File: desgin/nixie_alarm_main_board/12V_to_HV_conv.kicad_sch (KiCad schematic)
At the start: 19 parts, among them IC1 LM3488MM, IC5 TPH5200FNH, IC8 MCP4018T-502E_LT

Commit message: filter caps
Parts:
- added R42, R43: 5.1kΩ, RESC2012X60N, symbol SamacSys_Parts:ERJ-UP6D5101V
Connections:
- net +12V: now also L2.1
- net +3.3V: now also R42.2, R43.2
- net DPOT_SCL: now also R42.1
- net DPOT_SDA: now also R43.1
- net at IC1.1 (ISEN), R13.1: no longer L2.1
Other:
- moved on the sheet: C10, D1, L2

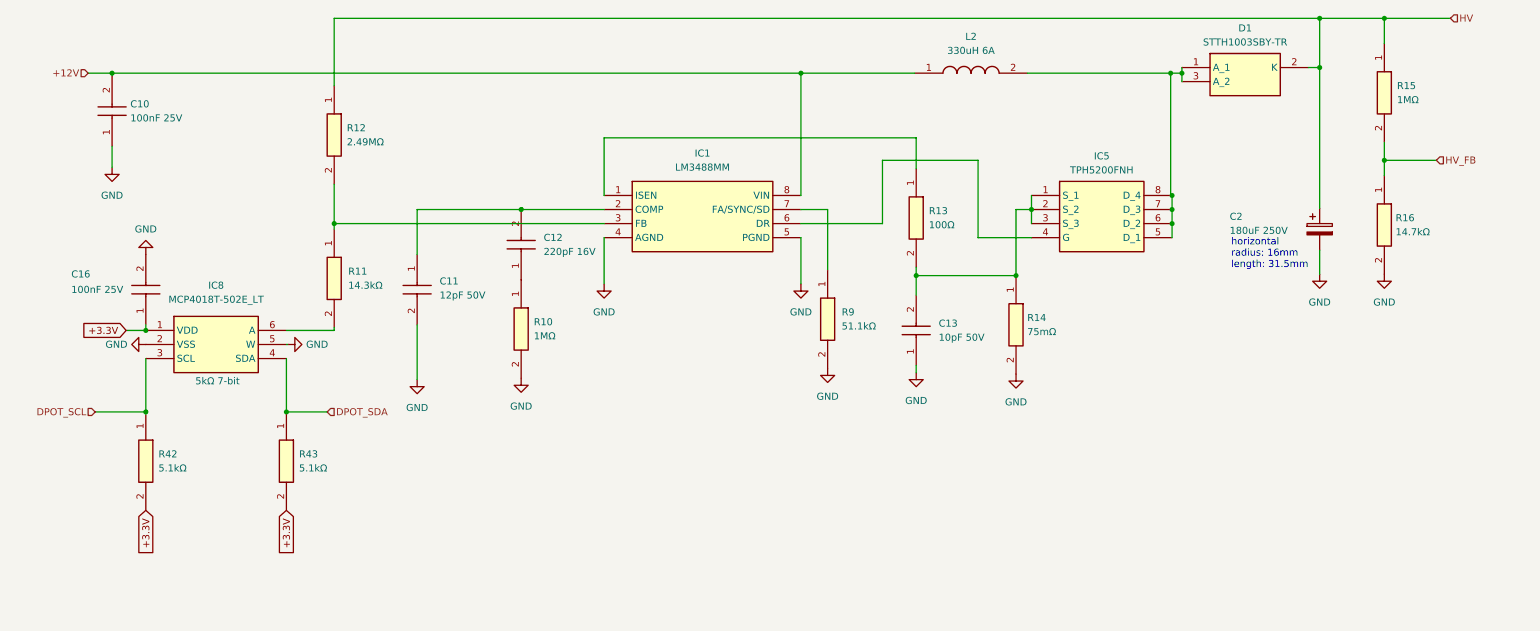
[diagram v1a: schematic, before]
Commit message: new rezistors
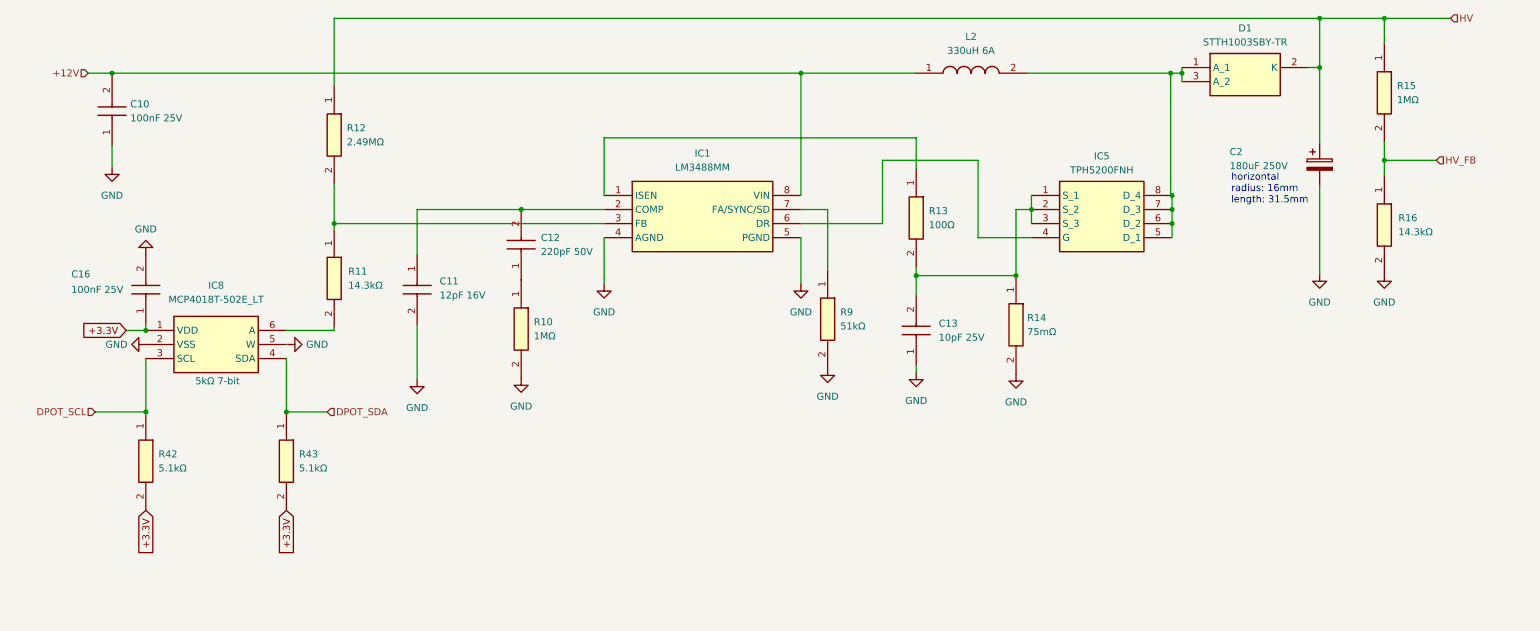
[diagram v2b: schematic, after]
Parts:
- C10, C16: footprint GRM033D70J224ME01D -> Capacitor_SMD:C_0805_2012Metric_Pad1.18x1.45mm_HandSolder
- C11: value 12pF 50V -> 12pF 16V
- C12: value 220pF 16V -> 220pF 50V; footprint GRM033D70J224ME01D -> Capacitor_SMD:C_0805_2012Metric_Pad1.18x1.45mm_HandSolder
- C13: value 10pF 50V -> 10pF 25V; footprint GRM033D70J224ME01D -> Capacitor_SMD:C_0805_2012Metric_Pad1.18x1.45mm_HandSolder
- R10, R12, R15: footprint RESC1005X40N -> Resistor_SMD:R_1206_3216Metric_Pad1.30x1.75mm_HandSolder
- R11: footprint RESC1005X40N -> Resistor_SMD:R_0805_2012Metric_Pad1.20x1.40mm_HandSolder
- R14: footprint ERJUP6 -> Resistor_SMD:R_0805_2012Metric_Pad1.20x1.40mm_HandSolder
- R16: value 14.7kΩ -> 14.3kΩ; footprint RESC1005X40N -> Resistor_SMD:R_0805_2012Metric_Pad1.20x1.40mm_HandSolder
- R42, R43: footprint RESC2012X60N -> Resistor_SMD:R_0805_2012Metric_Pad1.20x1.40mm_HandSolder
- R9: value 51.1kΩ -> 51kΩ; footprint RESC1005X40N -> Resistor_SMD:R_0805_2012Metric_Pad1.20x1.40mm_HandSolder
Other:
- moved on the sheet: C2
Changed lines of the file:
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@@
 	)
 	(junction
-		(at 247.904 52.324)
-		(diameter 0)
-		(color 0 0 0 0)
-	)
-	(junction
 		(at 29.718 53.34)
 		(diameter 0)
@@
 	)
 	(junction
+		(at 247.904 52.324)
+		(diameter 0)
+		(color 0 0 0 0)
+	)
+	(junction
 		(at 259.588 69.088)
 		(diameter 0)
@@
 	(wire
 		(pts
-			(xy 247.904 85.344) (xy 247.904 89.662)
+			(xy 247.904 73.66) (xy 247.904 89.662)
 		)
 		(stroke
@@
 	(wire
 		(pts
-			(xy 247.904 52.324) (xy 247.904 77.724)
+			(xy 247.904 52.324) (xy 247.904 66.04)
 		)
 		(stroke
@@
 	(text "horizontal\nradius: 16mm\nlength: 31.5mm\n"
 		(exclude_from_sim no)
-		(at 231.902 85.9791 0)
+		(at 231.902 74.2951 0)
 		(effects
 			(font
@@
 		(on_board yes)
 		(dnp no)
-		(fields_autoplaced yes)
 		(property "Reference" "C12"
-			(at 107.696 83.0579 90)
+			(at 107.188 83.058 90)
 			(effects
 				(font
@@
 			)
 		)
-		(property "Value" "220pF 16V"
-			(at 107.696 85.5979 90)
+		(property "Value" "220pF 50V"
+			(at 107.188 85.598 90)
 			(effects
 				(font
@@
 			)
 		)
-		(property "Footprint" "GRM033D70J224ME01D"
+		(property "Footprint" "Capacitor_SMD:C_0805_2012Metric_Pad1.18x1.45mm_HandSolder"
 			(at 199.822 81.788 0)
 			(effects
@@
 		(fields_autoplaced yes)
 		(property "Reference" "R9"
-			(at 161.544 96.5199 90)
+			(at 161.29 96.5199 90)
 			(effects
 				(font
@@
 			)
 		)
-		(property "Value" "51.1kΩ"
-			(at 161.544 99.0599 90)
+		(property "Value" "51kΩ"
+			(at 161.29 99.0599 90)
 			(effects
 				(font
@@
 			)
 		)
-		(property "Footprint" "RESC1005X40N"
+		(property "Footprint" "Resistor_SMD:R_0805_2012Metric_Pad1.20x1.40mm_HandSolder"
 			(at 62.814 102.87 0)
 			(effects
@@
 			)
 		)
-		(property "Footprint" "RESC2012X60N"
+		(property "Footprint" "Resistor_SMD:R_0805_2012Metric_Pad1.20x1.40mm_HandSolder"
 			(at -34.976 128.524 0)
 			(effects
@@
 			)
 		)
-		(property "Footprint" "RESC1005X40N"
+		(property "Footprint" "Resistor_SMD:R_1206_3216Metric_Pad1.30x1.75mm_HandSolder"
 			(at 7.442 104.648 0)
 			(effects
@@
 	(symbol
 		(lib_id "Device:C_Polarized")
-		(at 247.904 81.534 0)
+		(at 247.904 69.85 0)
 		(unit 1)
 		(exclude_from_sim no)
@@
 		(dnp no)
 		(property "Reference" "C2"
-			(at 231.648 79.248 0)
+			(at 231.648 67.564 0)
 			(effects
 				(font
@@
 		)
 		(property "Value" "180uF 250V"
-			(at 231.648 81.788 0)
+			(at 231.648 70.104 0)
 			(effects
 				(font
@@
 		)
 		(property "Footprint" "Capacitor_THT:CP_Radial_D10.0mm_P7.50mm"
-			(at 248.8692 85.344 0)
+			(at 248.8692 73.66 0)
 			(effects
 				(font
@@
 		)
 		(property "Datasheet" "~"
-			(at 247.904 81.534 0)
+			(at 247.904 69.85 0)
 			(effects
 				(font
@@
 		)
 		(property "Description" "Polarized capacitor"
-			(at 247.904 81.534 0)
+			(at 247.904 69.85 0)
 			(effects
 				(font
@@
 	)
 	(symbol
+		(lib_id "SamacSys_Parts:CRCW04022K74FKED")
+		(at 259.588 71.882 270)
+		(unit 1)
+		(exclude_from_sim no)
+		(in_bom yes)
+		(on_board yes)
+		(dnp no)
+		(fields_autoplaced yes)
+		(property "Reference" "R16"
+			(at 262.128 79.5019 90)
+			(effects
+				(font
+					(size 1.27 1.27)
+				)
+				(justify left)
+			)
+		)
+		(property "Value" "14.3kΩ"
+			(at 262.128 82.0419 90)
+			(effects
+				(font
+					(size 1.27 1.27)
+				)
+				(justify left)
+			)
+		)
+		(property "Footprint" "Resistor_SMD:R_0805_2012Metric_Pad1.20x1.40mm_HandSolder"
+			(at 163.398 85.852 0)
+			(effects
+				(font
+					(size 1.27 1.27)
+				)
+				(justify left top)
+				(hide yes)
+			)
+		)
+		(property "Datasheet" "http://www.vishay.com/docs/20035/dcrcwe3.pdf"
+			(at 63.398 85.852 0)
+			(effects
+				(font
+					(size 1.27 1.27)
+				)
+				(justify left top)
+				(hide yes)
+			)
+		)
+		(property "Description" "CRCW0402 Resistor T/R 0.063W,1%,2K74 Vishay CRCW Series Thick Film Surface Mount Resistor 0402 Case 2.74k?? ??1% 0.063W ??100ppm/??C"
+			(at 259.588 71.882 0)
+			(effects
+				(font
+					(size 1.27 1.27)
+				)
+				(hide yes)
+			)
+		)
+		(property "Height" "0.4"
+			(at -136.602 85.852 0)
+			(effects
+				(font
+					(size 1.27 1.27)
+				)
+				(justify left top)
+				(hide yes)
+			)
+		)
+		(property "Mouser Part Number" "71-CRCW0402-2.74K-E3"
+			(at -236.602 85.852 0)
+			(effects
+				(font
+					(size 1.27 1.27)
+				)
+				(justify left top)
+				(hide yes)
+			)
+		)
+		(property "Mouser Price/Stock" "https://www.mouser.co.uk/ProductDetail/Vishay-Dale/CRCW04022K74FKED?qs=hD42E%2F8yzjqhiq0MwGcz5A%3D%3D"
+			(at -336.602 85.852 0)
+			(effects
+				(font
+					(size 1.27 1.27)
+				)
+				(justify left top)
+				(hide yes)
+			)
+		)
+		(property "Manufacturer_Name" "Vishay"
+			(at -436.602 85.852 0)
+			(effects
+				(font
+					(size 1.27 1.27)
+				)
+				(justify left top)
+				(hide yes)
+			)
+		)
+		(property "Manufacturer_Part_Number" "CRCW04022K74FKED"
+			(at -536.602 85.852 0)
+			(effects
+				(font
+					(size 1.27 1.27)
+				)
+				(justify left top)
+				(hide yes)
+			)
+		)
+		(pin "2"
+		)
+		(pin "1"
+		)
+		(instances
+			(project "nixie_alarm_main_board"
+				(path "/a0d555d7-39a0-4a98-b831-70d97d0aa5a1/01ca46d9-e95c-45f3-8c2d-e16b8652cb7d"
+					(reference "R16")
+					(unit 1)
+				)
+			)
+		)
+	)
+	(symbol
 		(lib_id "power:GND")
 		(at 118.618 91.44 0)
@@
 			)
 		)
-		(property "Value" "10pF 50V"
+		(property "Value" "10pF 25V"
 			(at 179.07 101.0919 90)
 			(effects
@@
 			)
 		)
-		(property "Footprint" "GRM033D70J224ME01D"
+		(property "Footprint" "Capacitor_SMD:C_0805_2012Metric_Pad1.18x1.45mm_HandSolder"
 			(at 271.196 97.282 0)
 			(effects
@@
 			)
 		)
-		(property "Footprint" "RESC1005X40N"
+		(property "Footprint" "Resistor_SMD:R_1206_3216Metric_Pad1.30x1.75mm_HandSolder"
 			(at -26.34 69.596 0)
 			(effects
@@
 			)
 		)
-		(property "Footprint" "RESC1005X40N"
+		(property "Footprint" "Resistor_SMD:R_0805_2012Metric_Pad1.20x1.40mm_HandSolder"
 			(at -26.34 95.504 0)
 			(effects
@@
 	)
 	(symbol
-		(lib_id "SamacSys_Parts:CRCW04022K74FKED")
-		(at 259.588 71.882 270)
-		(unit 1)
-		(exclude_from_sim no)
-		(in_bom yes)
-		(on_board yes)
-		(dnp no)
-		(fields_autoplaced yes)
-		(property "Reference" "R16"
-			(at 261.62 79.5019 90)
-			(effects
-				(font
-					(size 1.27 1.27)
-				)
-				(justify left)
-			)
-		)
-		(property "Value" "14.7kΩ"
-			(at 261.62 82.0419 90)
-			(effects
-				(font
-					(size 1.27 1.27)
-				)
-				(justify left)
-			)
-		)
-		(property "Footprint" "RESC1005X40N"
-			(at 163.398 85.852 0)
-			(effects
-				(font
-					(size 1.27 1.27)
-				)
-				(justify left top)
-				(hide yes)
-			)
-		)
-		(property "Datasheet" "http://www.vishay.com/docs/20035/dcrcwe3.pdf"
-			(at 63.398 85.852 0)
-			(effects
-				(font
-					(size 1.27 1.27)
-				)
-				(justify left top)
-				(hide yes)
-			)
-		)
-		(property "Description" "CRCW0402 Resistor T/R 0.063W,1%,2K74 Vishay CRCW Series Thick Film Surface Mount Resistor 0402 Case 2.74k?? ??1% 0.063W ??100ppm/??C"
-			(at 259.588 71.882 0)
-			(effects
-				(font
-					(size 1.27 1.27)
-				)
-				(hide yes)
-			)
-		)
-		(property "Height" "0.4"
-			(at -136.602 85.852 0)
-			(effects
-				(font
-					(size 1.27 1.27)
-				)
-				(justify left top)
-				(hide yes)
-			)
-		)
-		(property "Mouser Part Number" "71-CRCW0402-2.74K-E3"
-			(at -236.602 85.852 0)
-			(effects
-				(font
-					(size 1.27 1.27)
-				)
-				(justify left top)
-				(hide yes)
-			)
-		)
-		(property "Mouser Price/Stock" "https://www.mouser.co.uk/ProductDetail/Vishay-Dale/CRCW04022K74FKED?qs=hD42E%2F8yzjqhiq0MwGcz5A%3D%3D"
-			(at -336.602 85.852 0)
-			(effects
-				(font
-					(size 1.27 1.27)
-				)
-				(justify left top)
-				(hide yes)
-			)
-		)
-		(property "Manufacturer_Name" "Vishay"
-			(at -436.602 85.852 0)
-			(effects
-				(font
-					(size 1.27 1.27)
-				)
-				(justify left top)
-				(hide yes)
-			)
-		)
-		(property "Manufacturer_Part_Number" "CRCW04022K74FKED"
-			(at -536.602 85.852 0)
-			(effects
-				(font
-					(size 1.27 1.27)
-				)
-				(justify left top)
-				(hide yes)
-			)
-		)
-		(pin "2"
-		)
-		(pin "1"
-		)
-		(instances
-			(project "nixie_alarm_main_board"
-				(path "/a0d555d7-39a0-4a98-b831-70d97d0aa5a1/01ca46d9-e95c-45f3-8c2d-e16b8652cb7d"
-					(reference "R16")
-					(unit 1)
-				)
-			)
-		)
-	)
-	(symbol
 		(lib_id "SamacSys_Parts:GRM033R71E101KA01J")
 		(at 35.814 98.806 90)
@@
 			)
 		)
-		(property "Footprint" "GRM033D70J224ME01D"
+		(property "Footprint" "Capacitor_SMD:C_0805_2012Metric_Pad1.18x1.45mm_HandSolder"
 			(at 132.004 89.916 0)
 			(effects
@@
 			)
 		)
-		(property "Footprint" "RESC1005X40N"
+		(property "Footprint" "Resistor_SMD:R_1206_3216Metric_Pad1.30x1.75mm_HandSolder"
 			(at 163.398 61.976 0)
 			(effects
@@
 			)
 		)
-		(property "Footprint" "RESC2012X60N"
+		(property "Footprint" "Resistor_SMD:R_0805_2012Metric_Pad1.20x1.40mm_HandSolder"
 			(at -60.376 128.524 0)
 			(effects
@@
 			)
 		)
-		(property "Value" "12pF 50V"
+		(property "Value" "12pF 16V"
 			(at 88.9 93.4719 90)
 			(effects
@@
 			)
 		)
-		(property "Datasheet" "https://content.kemet.com/datasheets/KEM_C1002_X7R_SMD.pdf"
+		(property "Datasheet" "Capacitor_SMD:C_0805_2012Metric_Pad1.18x1.45mm_HandSolder"
 			(at -111.354 94.996 0)
 			(effects
@@
 			)
 		)
-		(property "Footprint" "ERJUP6"
+		(property "Footprint" "Resistor_SMD:R_0805_2012Metric_Pad1.20x1.40mm_HandSolder"
 			(at 96.85 103.886 0)
 			(effects
@@
 			)
 		)
-		(property "Footprint" "GRM033D70J224ME01D"
+		(property "Footprint" "Capacitor_SMD:C_0805_2012Metric_Pad1.18x1.45mm_HandSolder"
 			(at 125.908 57.658 0)
 			(effects

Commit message: new hv conv desgin
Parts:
- removed C2: 180uF 250V, Capacitor_THT:CP_Radial_D10.0mm_P7.50mm, symbol Device:C_Polarized
- removed D1: STTH1003SBY-TR, STTH1003SBYTR, symbol SamacSys_Parts:STTH1003SBY-TR
- removed IC5: TPH5200FNH, footprints:SOP Advance_TOS-L, symbol SamacSys_Parts:IRF8707TRPBF
- removed R9: 51kΩ, Resistor_SMD:R_0805_2012Metric_Pad1.20x1.40mm_HandSolder, symbol SamacSys_Parts:CRCW04022K74FKED
- added C26: 4.7uF 450V, ECWFE2W475K, symbol SamacSys_Parts:ECW-FE2W475K
- added D2: ES1G, DIOM5227X260N, symbol SamacSys_Parts:ES1G
- added Q8: STL2N80K5, STL2N80K5, symbol SamacSys_Parts:STL2N80K5
- added R44: 27kΩ, Resistor_SMD:R_0805_2012Metric_Pad1.20x1.40mm_HandSolder, symbol SamacSys_Parts:RK73H2ATTE1003F
- L2: value 330uH 6A -> 180uH 0.9A 6.3mΩ; footprint INDPM250280X2050N -> Inductor_SMD:L_12x12mm_H6mm
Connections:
- net GND: now also C26.2, R44.2
- net HV: now also C26.1, D2.1 (K)
- net at L2.2: now also D2.2 (A), Q8.3 (D)
- net at IC1.7 (FA/SYNC/SD): now also R44.1
- net at C13.2, R13.2, R14.1: now also Q8.1 (S)
- net at IC1.6 (DR): now also Q8.2 (G)
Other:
- note removed: "horizontal radius: 16mm length: 31.5mm"
- moved on the sheet: R14

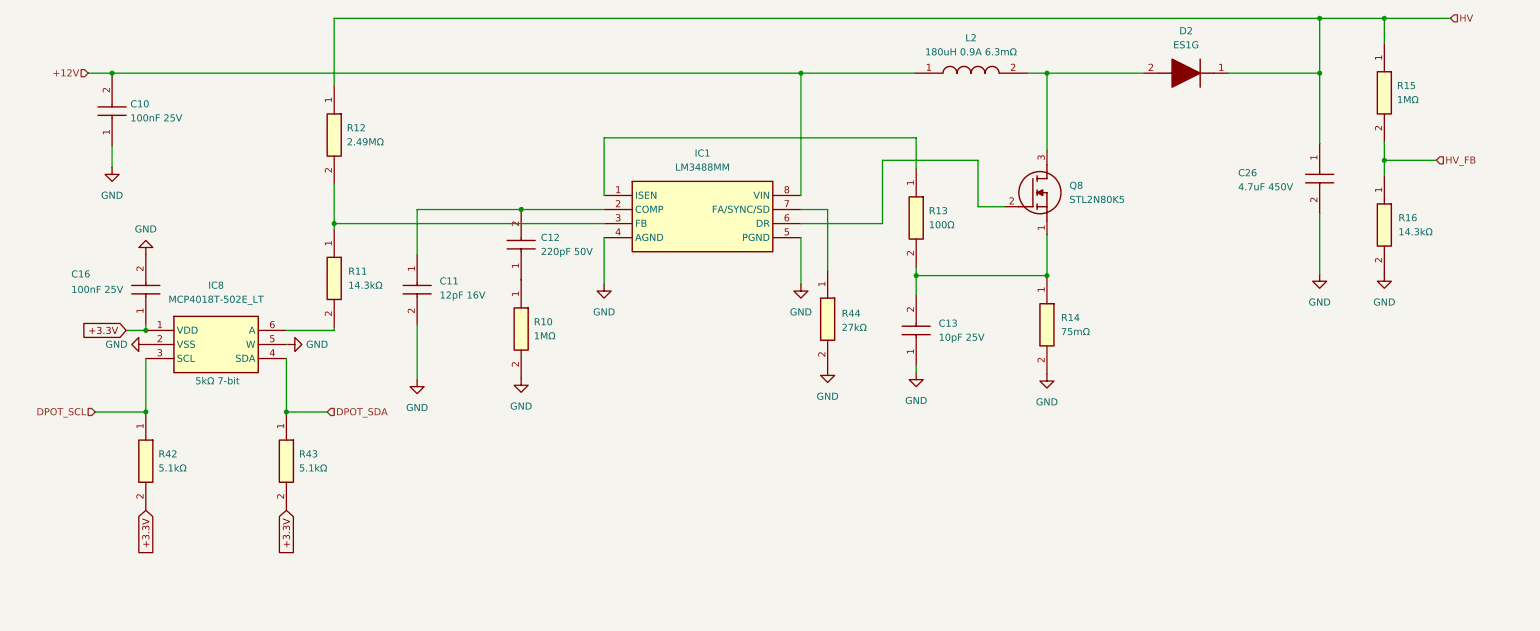
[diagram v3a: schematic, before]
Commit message: traces for nixie tubes
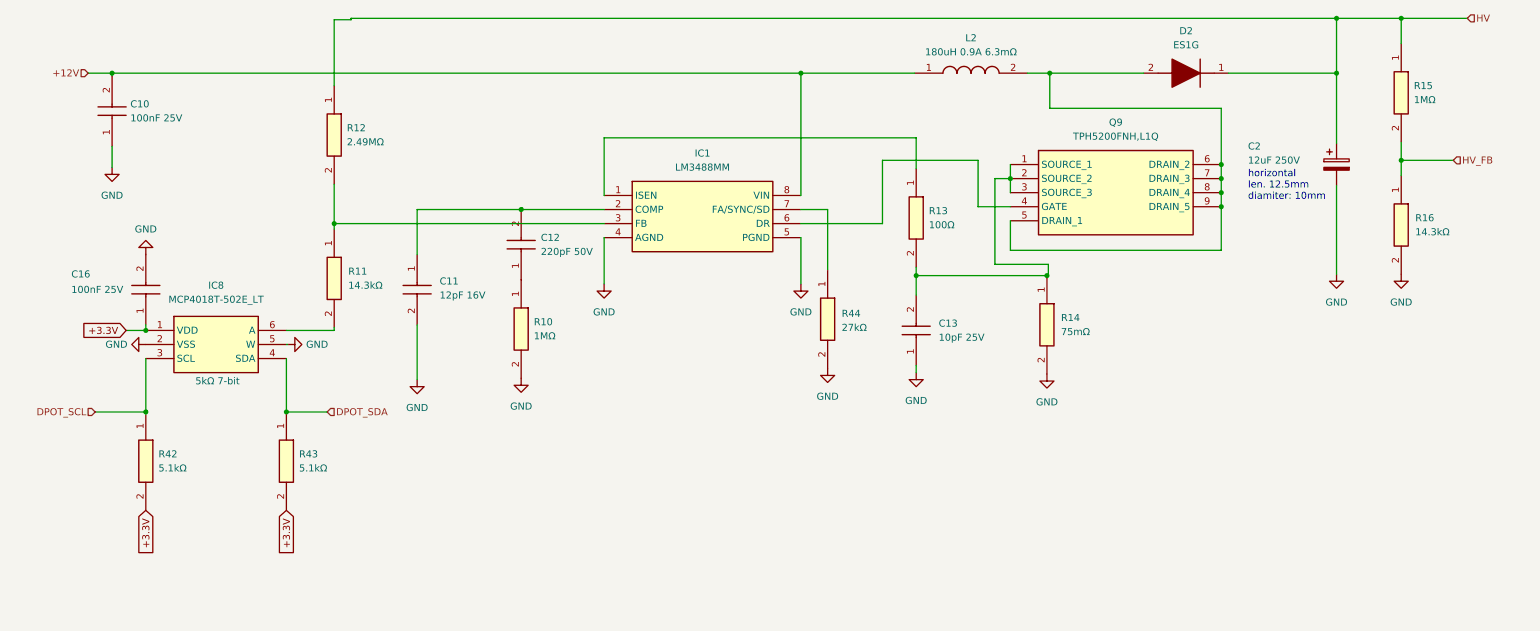
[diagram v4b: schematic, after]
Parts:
- removed C26: 4.7uF 450V, ECWFE2W475K, symbol SamacSys_Parts:ECW-FE2W475K
- removed Q8: STL2N80K5, STL2N80K5, symbol SamacSys_Parts:STL2N80K5
- added C2: 12uF 250V, Capacitor_THT:CP_Radial_D10.0mm_P5.00mm, symbol Device:C_Polarized
- added Q9: TPH5200FNH,L1Q, Package_SO:SO-8_3.9x4.9mm_P1.27mm, symbol SamacSys_Parts:TPH1110FNH,L1Q
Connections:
- net GND: now also C2.2
- net HV: now also C2.1
- net at D2.2 (A), L2.2: now also Q9.5 (DRAIN_1), Q9.6 (DRAIN_2), Q9.7 (DRAIN_3), Q9.8 (DRAIN_4), Q9.9 (DRAIN_5)
- net at C13.2, R13.2, R14.1: now also Q9.1 (SOURCE_1), Q9.2 (SOURCE_2), Q9.3 (SOURCE_3)
- net at IC1.6 (DR): now also Q9.4 (GATE)
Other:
- note added: "horizontal len. 12.5mm diamiter: 10mm"
- moved on the sheet: R15, R16

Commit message: all components in board footprint
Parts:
- R13: footprint RESC1005X40N -> Resistor_SMD:R_0805_2012Metric_Pad1.20x1.40mm_HandSolder
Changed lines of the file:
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@@
 			)
 		)
-		(property "Footprint" "RESC1005X40N"
+		(property "Footprint" "Resistor_SMD:R_0805_2012Metric_Pad1.20x1.40mm_HandSolder"
 			(at 78.816 84.582 0)
 			(effects

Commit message: new layout
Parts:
- removed Q9: TPH5200FNH,L1Q, Package_SO:SO-8_3.9x4.9mm_P1.27mm, symbol SamacSys_Parts:TPH1110FNH,L1Q
- added Q8: TPH5200FNH,L1Q, TPHR6503PL1LQ, symbol SamacSys_Parts:TPHR6503PL1,LQ
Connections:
- net at D2.2 (A), L2.2: now also Q8.5 (D_1), Q8.6 (D_2), Q8.7 (D_3), Q8.8 (D_4), Q8.9 (D_5)
- net at C13.2, R13.2, R14.1: now also Q8.1 (S_1), Q8.2 (S_2), Q8.3 (S_3)
- net at IC1.6 (DR): now also Q8.4 (G)

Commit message: fixes added
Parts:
- added R5: 0Ω, Resistor_SMD:R_0805_2012Metric_Pad1.20x1.40mm_HandSolder, symbol SamacSys_Parts:CRCW04022K74FKED
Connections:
- net HV: now also R5.2; no longer C2.1, D2.1 (K), R12.1
- new net: C2.1, D2.1 (K), R12.1, R5.1
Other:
- moved on the sheet: C10, C11, C12, C13, C16, C2, D2, IC1, IC8, L2, Q8, R10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
